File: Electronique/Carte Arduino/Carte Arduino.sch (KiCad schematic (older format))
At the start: 11 parts

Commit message: Electronique/Carte Arduino/Carte Arduino.sch : - Ajout de l'Arduino
Electronique/Librairies kiCAD/Arduino.lib :
- Finition de la modélisation du schéma de l'arduino mini
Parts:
- added U?: ARDUINO_MINI, symbol ARDUINO_MINI
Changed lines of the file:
@@
-EESchema Schematic File Version 2  date 11/12/2011 09:01:38
+EESchema Schematic File Version 2  date 11/12/2011 11:45:20
 LIBS:power
 LIBS:device
@@
 LIBS:contrib
 LIBS:valves
+LIBS:Arduino
 LIBS:Carte Arduino-cache
 EELAYER 25  0
@@
 Sheet 1 1
 Title ""
-Date "10 dec 2011"
+Date "11 dec 2011"
 Rev ""
 Comp ""
@@
 Comment4 ""
 $EndDescr
+$Comp
+L ARDUINO_MINI U?
+U 1 1 4EE489A2
+P 6800 2000
+F 0 "U?" H 6800 2000 60  0000 C CNN
+F 1 "ARDUINO_MINI" H 6800 2000 60  0000 C CNN
+	1    6800 2000
+	1    0    0    -1
+$EndComp
 Text Notes 1850 4200 1    60   ~ 0
 Capteur temperature exterieure

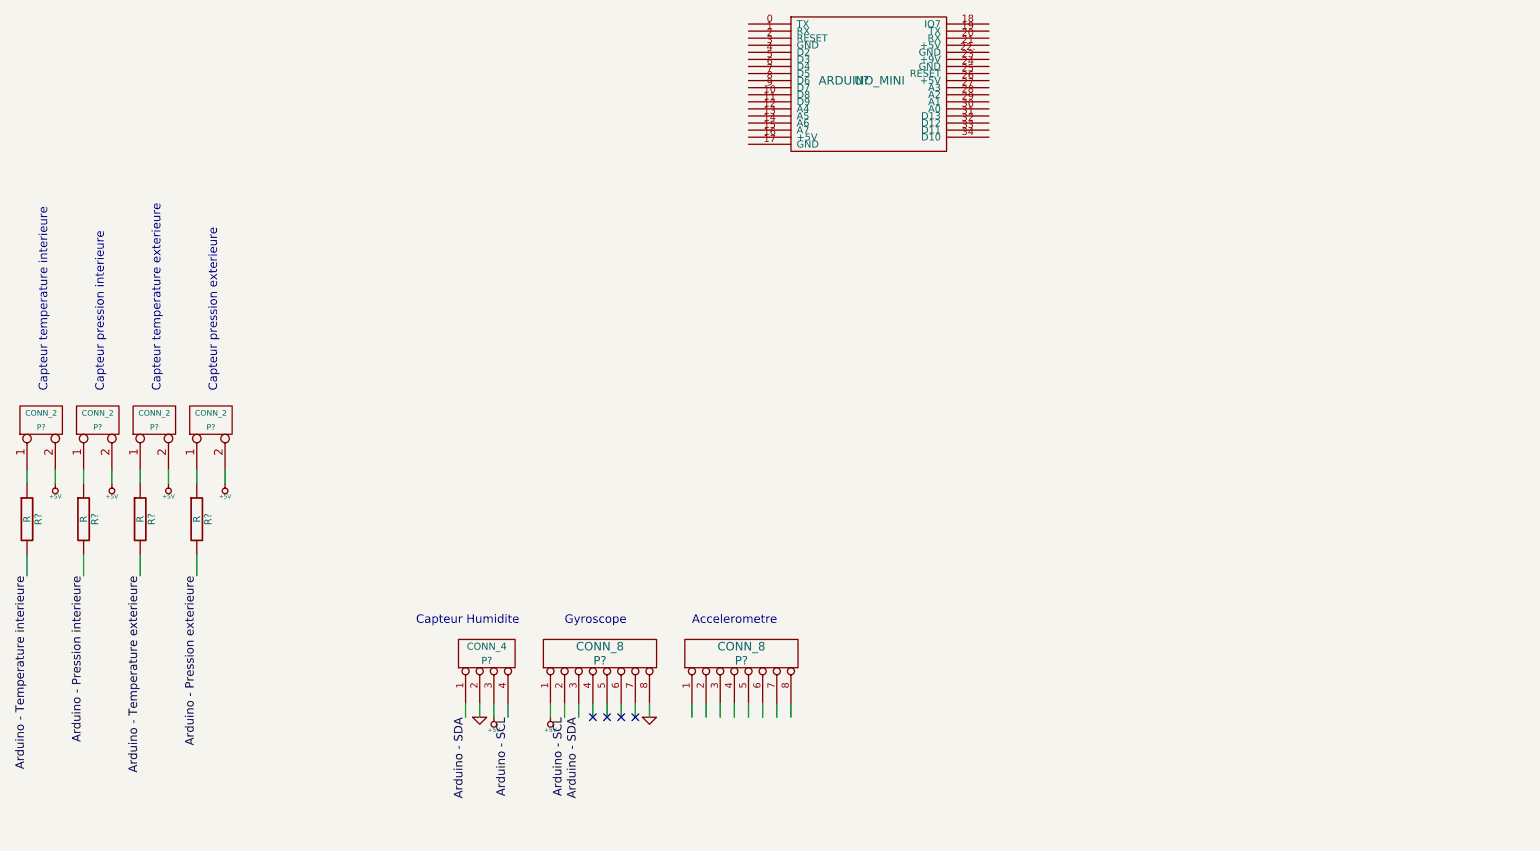
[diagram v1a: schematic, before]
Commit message: Electronique/Carte Arduino/Carte Arduino.sch : - Ajout de labels sur l'Arduino
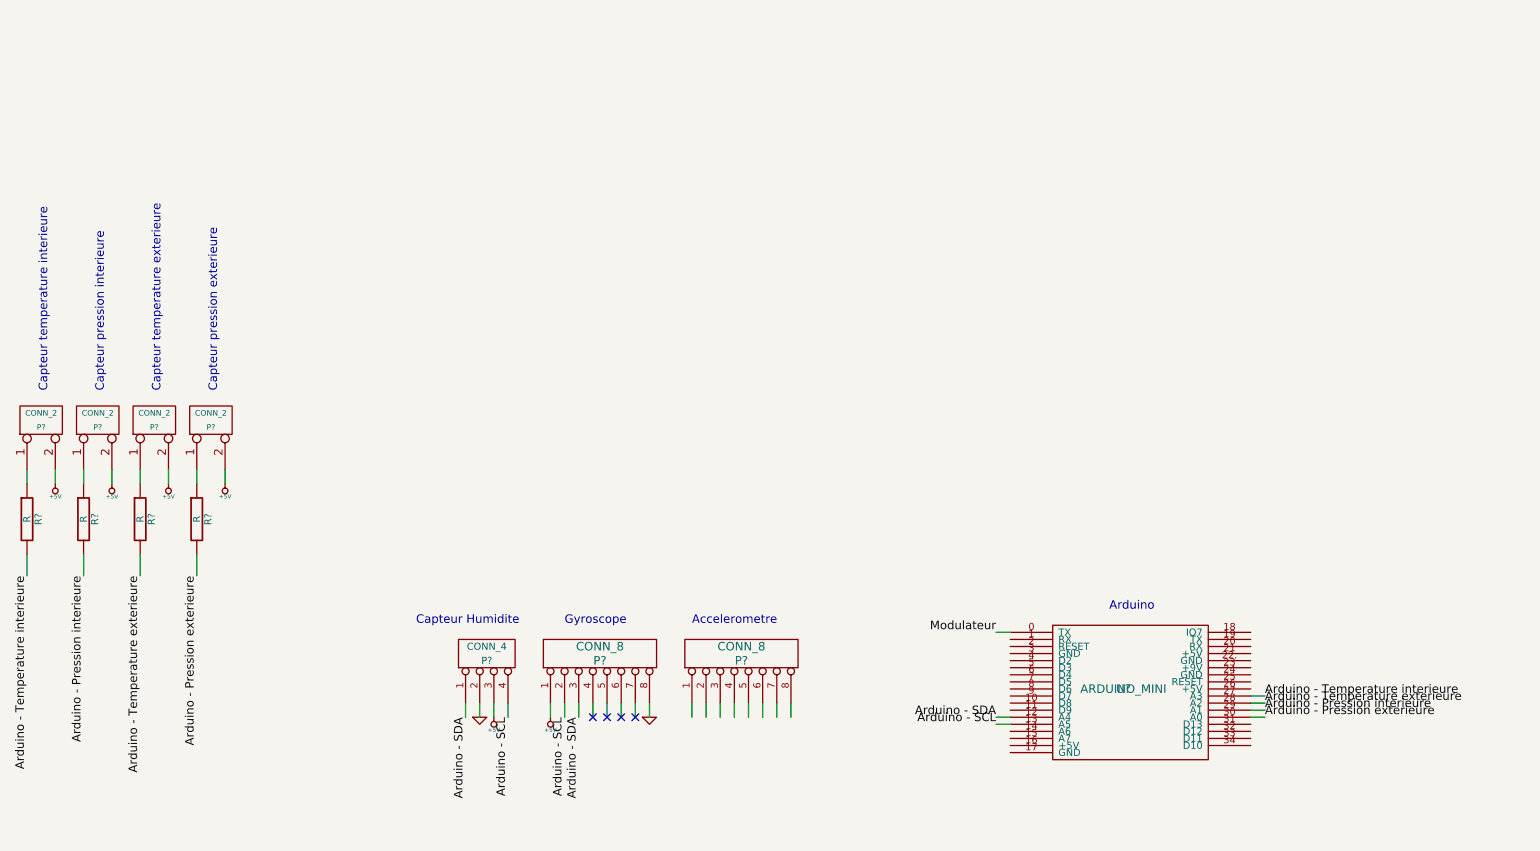
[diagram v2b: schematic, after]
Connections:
- net labels added: Modulateur
- wire segments 32 -> 39
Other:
- note added: "Arduino"
- moved on the sheet: U?
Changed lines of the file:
@@
-EESchema Schematic File Version 2  date 11/12/2011 11:45:20
+EESchema Schematic File Version 2  date 12/12/2011 18:19:07
 LIBS:power
 LIBS:device
@@
 Sheet 1 1
 Title ""
-Date "11 dec 2011"
+Date "12 dec 2011"
 Rev ""
 Comp ""
@@
 Comment4 ""
 $EndDescr
+Text Notes 8550 5750 0    60   ~ 0
+Arduino
+Wire Wire Line
+	7750 6550 7850 6550
+Wire Wire Line
+	9550 6350 9650 6350
+Wire Wire Line
+	9550 6450 9650 6450
+Wire Wire Line
+	7850 5900 7750 5900
+Wire Wire Line
+	6100 6400 6100 6500
+Wire Wire Line
+	5900 6400 5900 6500
+Wire Wire Line
+	5700 6400 5700 6500
+Wire Wire Line
+	5300 6400 5300 6500
+Wire Wire Line
+	5100 6400 5100 6500
+Wire Wire Line
+	4900 6400 4900 6500
+Wire Wire Line
+	4700 6400 4700 6500
+Wire Wire Line
+	4300 6400 4300 6500
+Wire Wire Line
+	4100 6400 4100 6500
+Wire Wire Line
+	2100 5350 2100 5500
+Wire Wire Line
+	2100 4750 2100 4850
+Wire Wire Line
+	2300 4850 2300 4750
+Wire Wire Line
+	1900 4850 1900 4750
+Wire Wire Line
+	1700 4750 1700 4850
+Wire Wire Line
+	1700 5350 1700 5500
+Wire Wire Line
+	1300 5350 1300 5500
+Wire Wire Line
+	1300 4750 1300 4850
+Wire Wire Line
+	1500 4850 1500 4750
+Wire Wire Line
+	1100 4850 1100 4750
+Wire Wire Line
+	900  4750 900  4850
+Wire Wire Line
+	900  5350 900  5500
+Wire Wire Line
+	4000 6400 4000 6500
+Wire Wire Line
+	4200 6400 4200 6500
+Wire Wire Line
+	4600 6400 4600 6500
+Wire Wire Line
+	4800 6400 4800 6500
+Wire Wire Line
+	5000 6400 5000 6500
+Wire Wire Line
+	5200 6400 5200 6500
+Wire Wire Line
+	5600 6400 5600 6500
+Wire Wire Line
+	5800 6400 5800 6500
+Wire Wire Line
+	6000 6400 6000 6500
+Wire Wire Line
+	6200 6400 6200 6500
+Wire Wire Line
+	6300 6400 6300 6500
+Wire Wire Line
+	9550 6500 9650 6500
+Wire Wire Line
+	9550 6400 9650 6400
+Wire Wire Line
+	7850 6500 7750 6500
+Text Label 7750 6550 2    60   ~ 0
+Arduino - SCL
+Text Label 7750 6500 2    60   ~ 0
+Arduino - SDA
+Text Label 7750 5900 2    60   ~ 0
+Modulateur
+Text Label 9650 6350 0    60   ~ 0
+Arduino - Temperature interieure
+Text Label 9650 6400 0    60   ~ 0
+Arduino - Temperature exterieure
+Text Label 9650 6450 0    60   ~ 0
+Arduino - Pression interieure
+Text Label 9650 6500 0    60   ~ 0
+Arduino - Pression exterieure
 $Comp
 L ARDUINO_MINI U?
 U 1 1 4EE489A2
-P 6800 2000
-F 0 "U?" H 6800 2000 60  0000 C CNN
-F 1 "ARDUINO_MINI" H 6800 2000 60  0000 C CNN
-	1    6800 2000
+P 8650 6300
+F 0 "U?" H 8650 6300 60  0000 C CNN
+F 1 "ARDUINO_MINI" H 8650 6300 60  0000 C CNN
+	1    8650 6300
 	1    0    0    -1
 $EndComp
@@
 Text Notes 5600 5850 0    60   ~ 0
 Accelerometre
-Wire Wire Line
-	6300 6400 6300 6500
-Wire Wire Line
-	6200 6400 6200 6500
-Wire Wire Line
-	6000 6400 6000 6500
-Wire Wire Line
-	5800 6400 5800 6500
-Wire Wire Line
-	5600 6400 5600 6500
-Wire Wire Line
-	5200 6400 5200 6500
-Wire Wire Line
-	5000 6400 5000 6500
-Wire Wire Line
-	4800 6400 4800 6500
-Wire Wire Line
-	4600 6400 4600 6500
-Wire Wire Line
-	4200 6400 4200 6500
-Wire Wire Line
-	4000 6400 4000 6500
-Wire Wire Line
-	900  5350 900  5500
-Wire Wire Line
-	900  4750 900  4850
-Wire Wire Line
-	1100 4850 1100 4750
-Wire Wire Line
-	1500 4850 1500 4750
-Wire Wire Line
-	1300 4750 1300 4850
-Wire Wire Line
-	1300 5350 1300 5500
-Wire Wire Line
-	1700 5350 1700 5500
-Wire Wire Line
-	1700 4750 1700 4850
-Wire Wire Line
-	1900 4850 1900 4750
-Wire Wire Line
-	2300 4850 2300 4750
-Wire Wire Line
-	2100 4750 2100 4850
-Wire Wire Line
-	2100 5350 2100 5500
-Wire Wire Line
-	4100 6400 4100 6500
-Wire Wire Line
-	4300 6400 4300 6500
-Wire Wire Line
-	4700 6400 4700 6500
-Wire Wire Line
-	4900 6400 4900 6500
-Wire Wire Line
-	5100 6400 5100 6500
-Wire Wire Line
-	5300 6400 5300 6500
-Wire Wire Line
-	5700 6400 5700 6500
-Wire Wire Line
-	5900 6400 5900 6500
-Wire Wire Line
-	6100 6400 6100 6500
 $Comp
 L CONN_8 P?
@@
 NoConn ~ 5100 6500
 $Comp
-L GND #PWR?
+L GND #PWR01
 U 1 1 4EE37BF2
 P 5300 6500
-F 0 "#PWR?" H 5300 6500 30  0001 C CNN
+F 0 "#PWR01" H 5300 6500 30  0001 C CNN
 F 1 "GND" H 5300 6430 30  0001 C CNN
 	1    5300 6500
@@
 Arduino - SCL
 $Comp
-L +5V #PWR?
+L +5V #PWR02
 U 1 1 4EE37B76
 P 4600 6500
-F 0 "#PWR?" H 4600 6590 20  0001 C CNN
+F 0 "#PWR02" H 4600 6590 20  0001 C CNN
 F 1 "+5V" H 4600 6590 30  0000 C CNN
 	1    4600 6500
@@
 $EndComp
 $Comp
-L GND #PWR?
+L GND #PWR03
 U 1 1 4EE3788C
 P 4100 6500
-F 0 "#PWR?" H 4100 6500 30  0001 C CNN
+F 0 "#PWR03" H 4100 6500 30  0001 C CNN
 F 1 "GND" H 4100 6430 30  0001 C CNN
 	1    4100 6500
@@
 $EndComp
 $Comp
-L +5V #PWR?
+L +5V #PWR04
 U 1 1 4EE3787E
 P 4200 6500
-F 0 "#PWR?" H 4200 6590 20  0001 C CNN
+F 0 "#PWR04" H 4200 6590 20  0001 C CNN
 F 1 "+5V" H 4200 6590 30  0000 C CNN
 	1    4200 6500
@@
 $EndComp
 $Comp
-L +5V #PWR?
+L +5V #PWR05
 U 1 1 4EE364FB
 P 2300 4850
-F 0 "#PWR?" H 2300 4940 20  0001 C CNN
+F 0 "#PWR05" H 2300 4940 20  0001 C CNN
 F 1 "+5V" H 2300 4940 30  0000 C CNN
 	1    2300 4850
@@
 $EndComp
 $Comp
-L +5V #PWR?
+L +5V #PWR06
 U 1 1 4EE364F6
 P 1900 4850
-F 0 "#PWR?" H 1900 4940 20  0001 C CNN
+F 0 "#PWR06" H 1900 4940 20  0001 C CNN
 F 1 "+5V" H 1900 4940 30  0000 C CNN
 	1    1900 4850
@@
 $EndComp
 $Comp
-L +5V #PWR?
+L +5V #PWR07
 U 1 1 4EE22ACD
 P 1500 4850
-F 0 "#PWR?" H 1500 4940 20  0001 C CNN
+F 0 "#PWR07" H 1500 4940 20  0001 C CNN
 F 1 "+5V" H 1500 4940 30  0000 C CNN
 	1    1500 4850
@@
 $EndComp
 $Comp
-L +5V #PWR?
+L +5V #PWR08
 U 1 1 4EE0BB2B
 P 1100 4850
-F 0 "#PWR?" H 1100 4940 20  0001 C CNN
+F 0 "#PWR08" H 1100 4940 20  0001 C CNN
 F 1 "+5V" H 1100 4940 30  0000 C CNN
 	1    1100 4850
